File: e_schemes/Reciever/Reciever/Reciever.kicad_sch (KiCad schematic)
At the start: 31 parts, among them J1 Conn_01x03, J2 Conn_01x03, Q1 AO3400A, SW1 SW_Push, SW2 SW_Push, SW3 SW_Reload, U1 ESP32-WROOM-32E

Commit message: ADD: Добавлены  электросхемы
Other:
- company: SF-DEV -> (none)
- title: Схема передатчика -> (none)
- moved on the sheet: C1, C2, C3, C4, C5, D1, D2, D3, D4, D5, D6, J1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

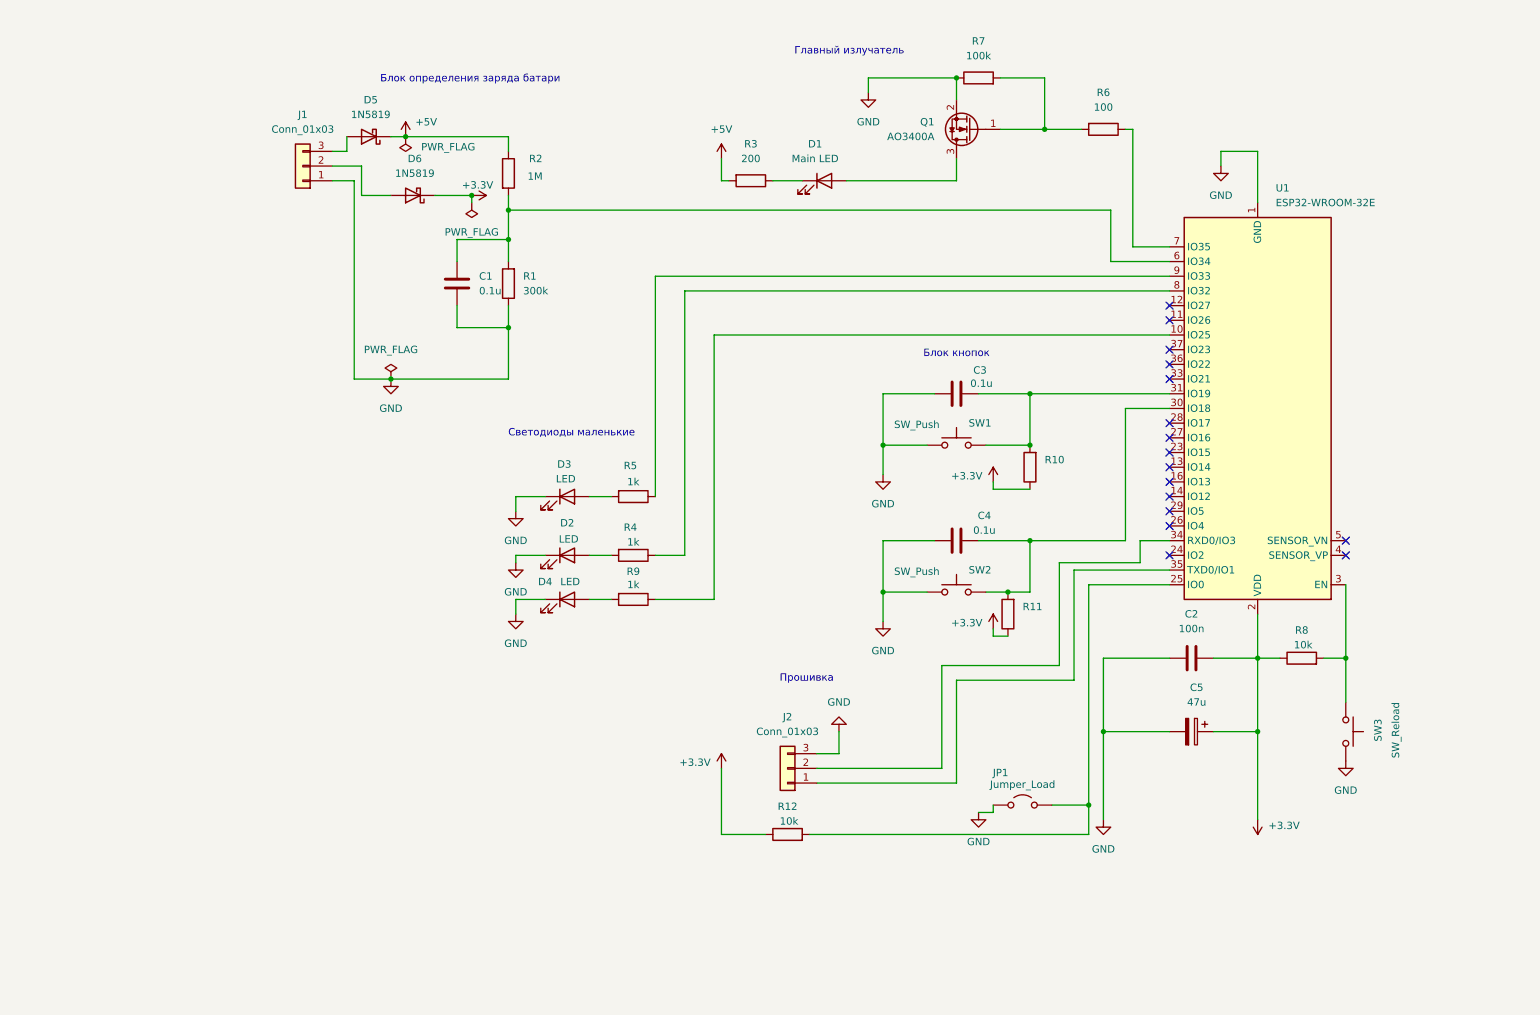
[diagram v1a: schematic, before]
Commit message: ADD:  Схема приемника
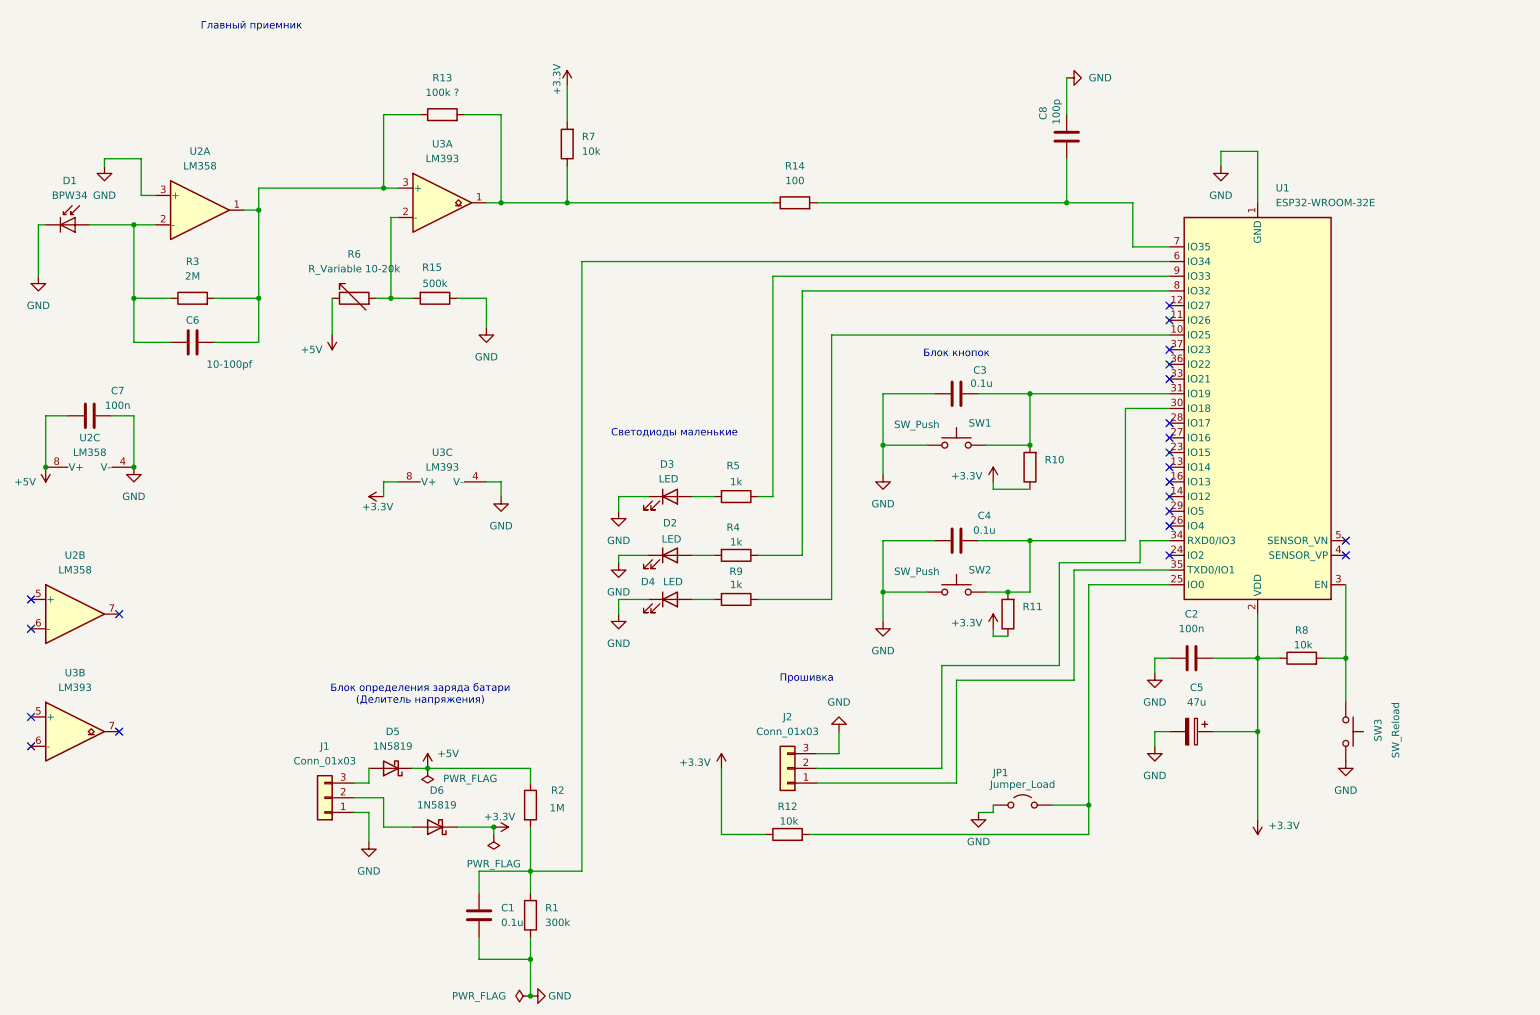
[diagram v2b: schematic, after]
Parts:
- removed D1: Main LED, OptoDevice:Osram_BPW82, symbol Device:LED
- removed Q1: AO3400A, Package_TO_SOT_SMD:SOT-23, symbol Transistor_FET:AO3400A
- removed R6: 100, Resistor_THT:R_Axial_DIN0204_L3.6mm_D1.6mm_P7.62mm_Horizontal, symbol Device:R
- added C6: 10-100pf, Capacitor_THT:C_Disc_D3.0mm_W1.6mm_P2.50mm, symbol Device:C
- added C7: 100n, Capacitor_THT:C_Disc_D3.0mm_W1.6mm_P2.50mm, symbol Device:C
- added C8: 100p, Capacitor_THT:C_Disc_D3.0mm_W1.6mm_P2.50mm, symbol Device:C
- added D1: BPW34, OptoDevice:Osram_DIL2_4.3x4.65mm_P5.08mm, symbol Sensor_Optical:BPW34
- added R13: 100k ?, symbol Device:R
- added R14: 100, symbol Device:R
- added R15: 500k, Resistor_THT:R_Axial_DIN0204_L3.6mm_D1.6mm_P7.62mm_Horizontal, symbol Device:R
- added R6: R_Variable 10-20k, symbol Device:R_Variable
- added U2: LM358, symbol Amplifier_Operational:LM358
- added U3: LM393, symbol Comparator:LM393
- R3: value 200 -> 2M; footprint Resistor_THT:R_Axial_DIN0204_L3.6mm_D1.6mm_P7.62mm_Horizontal -> (none)
- R7: value 100k -> 10k; footprint Resistor_THT:R_Axial_DIN0204_L3.6mm_D1.6mm_P7.62mm_Horizontal -> (none)
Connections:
- net +3.3V: now also R7.2, U3.8 (V+)
- net +5V: now also C7.1, R6.1, U2.8 (V+); no longer R3.2
- net GND: now also C7.2, C8.2, D1.1 (K), R15.1, U2.3 (+), U2.4 (V-), U3.4 (V-); no longer R7.1
- net at U1.7 (IO35): now also C8.1, R14.2
- net at R3.1: now also C6.1, D1.2 (A), U2.2 (-)
- new net: C6.2, R13.1, R3.2, U2.1, U3.3 (+)
- new net: R15.2, R6.2, U3.2 (-)
- new net: R13.2, R14.1, R7.1, U3.1
- no-connect marks 16 -> 22
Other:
- note added: "Блок определения заряда батари (Делитель напряжения)"
- note added: "Главный приемник"
- note removed: "Блок определения заряда батари"
- note removed: "Главный излучатель"
- moved on the sheet: C1, D2, D3, D4, D5, D6, J1, R1, R2, R4, R5, R9

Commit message: UPDATE: схема RX
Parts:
- R13, R14, R3, R6, R7: footprint (none) -> Resistor_THT:R_Axial_DIN0204_L3.6mm_D1.6mm_P7.62mm_Horizontal
- U1: footprint RF_Module:ESP32-WROOM-32E -> RF_Module:ESP32-WROOM-32UE
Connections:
- net at C8.1, R14.2: now also U1.16 (IO13); no longer U1.7 (IO35)
- no-connect marks 22 -> 21
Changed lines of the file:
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@@
 	)
 	(no_connect
-		(at 215.9 95.25)
-	)
-	(no_connect
 		(at 19.05 120.65)
 	)
@@
 	(wire
 		(pts
-			(xy 209.55 46.99) (xy 209.55 54.61)
+			(xy 215.9 95.25) (xy 209.55 95.25)
 		)
 		(stroke
@@
 	(wire
 		(pts
+			(xy 209.55 46.99) (xy 209.55 95.25)
+		)
+		(stroke
+			(width 0)
+			(type default)
+		)
+	)
+	(wire
+		(pts
 			(xy 175.26 80.01) (xy 166.37 80.01)
 		)
@@
 	(wire
 		(pts
-			(xy 209.55 54.61) (xy 215.9 54.61)
-		)
-		(stroke
-			(width 0)
-			(type default)
-		)
-	)
-	(wire
-		(pts
 			(xy 223.52 138.43) (xy 231.14 138.43)
 		)
@@
 			)
 		)
-		(property "Footprint" "RF_Module:ESP32-WROOM-32E"
+		(property "Footprint" "RF_Module:ESP32-WROOM-32UE"
 			(at 214.63 48.26 0)
 			(effects
@@
 			)
 		)
-		(property "Footprint" ""
+		(property "Footprint" "Resistor_THT:R_Axial_DIN0204_L3.6mm_D1.6mm_P7.62mm_Horizontal"
 			(at 151.13 48.768 90)
 			(effects
@@
 			)
 		)
-		(property "Footprint" ""
+		(property "Footprint" "Resistor_THT:R_Axial_DIN0204_L3.6mm_D1.6mm_P7.62mm_Horizontal"
 			(at 90.17 33.528 90)
 			(effects
@@
 			)
 		)
-		(property "Footprint" ""
+		(property "Footprint" "Resistor_THT:R_Axial_DIN0204_L3.6mm_D1.6mm_P7.62mm_Horizontal"
 			(at 74.93 65.278 90)
 			(effects
@@
 			)
 		)
-		(property "Footprint" ""
+		(property "Footprint" "Resistor_THT:R_Axial_DIN0204_L3.6mm_D1.6mm_P7.62mm_Horizontal"
 			(at 113.538 36.83 90)
 			(effects
@@
 			)
 		)
-		(property "Footprint" ""
+		(property "Footprint" "Resistor_THT:R_Axial_DIN0204_L3.6mm_D1.6mm_P7.62mm_Horizontal"
 			(at 46.99 65.278 90)
 			(effects

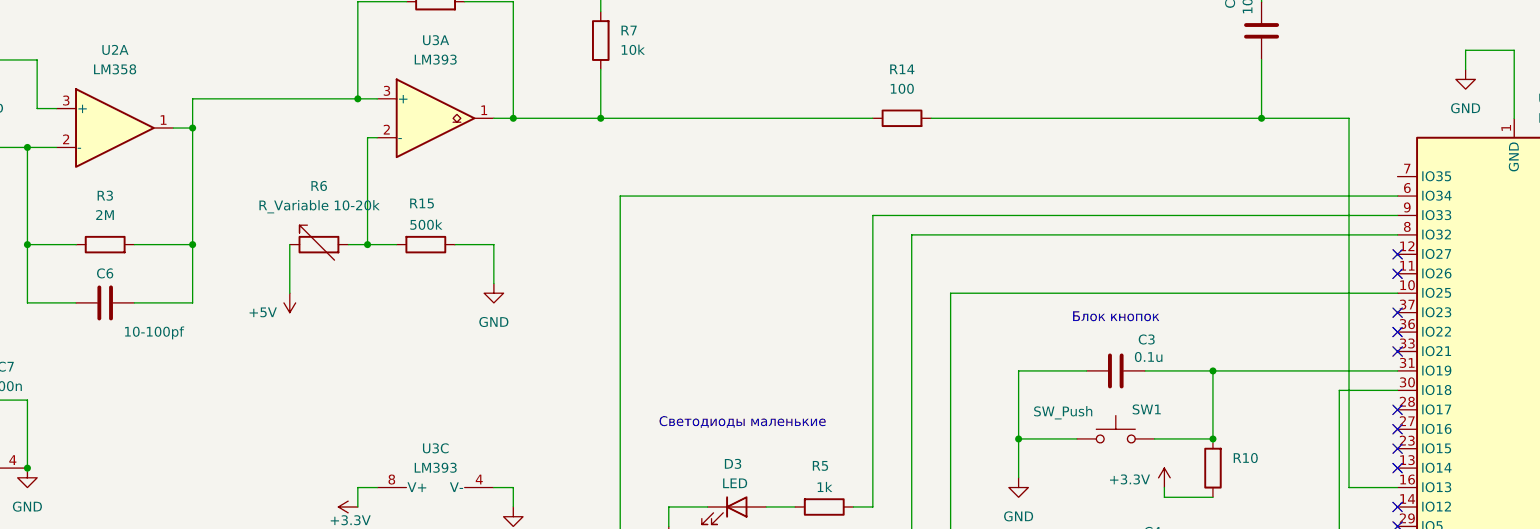
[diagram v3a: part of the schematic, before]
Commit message: Отрисовка схемы
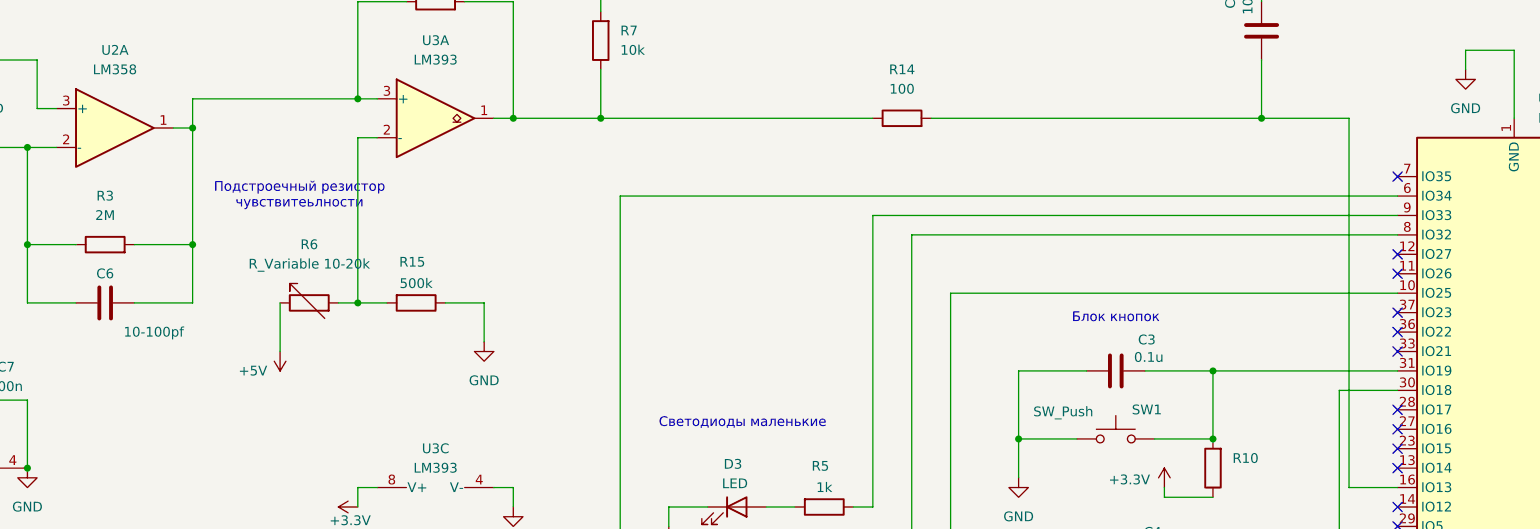
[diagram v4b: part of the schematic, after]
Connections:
- no-connect marks 21 -> 22
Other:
- note added: "Подстроечный резистор чувствитеьлности"
- moved on the sheet: R15, R6
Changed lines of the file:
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@@
 	(generator_version "9.0")
 	(paper "A4")
+	(text "Подстроечный резистор \nчувствитеьлности"
+		(exclude_from_sim no)
+		(at 72.39 57.15 0)
+		(effects
+			(font
+				(size 1.27 1.27)
+			)
+		)
+	)
 	(text "Блок определения заряда батари\n(Делитель напряжения)"
 		(exclude_from_sim no)
@@
 	)
 	(junction
-		(at 81.28 63.5)
+		(at 80.01 71.12)
 		(diameter 0)
 		(color 0 0 0 0)
@@
 	)
 	(no_connect
+		(at 215.9 54.61)
+	)
+	(no_connect
 		(at 215.9 87.63)
 	)
@@
 	(wire
 		(pts
-			(xy 78.74 63.5) (xy 81.28 63.5)
+			(xy 77.47 71.12) (xy 80.01 71.12)
 		)
 		(stroke
@@
 	(wire
 		(pts
-			(xy 81.28 63.5) (xy 85.09 63.5)
+			(xy 80.01 71.12) (xy 83.82 71.12)
 		)
 		(stroke
@@
 	(wire
 		(pts
-			(xy 97.79 68.58) (xy 97.79 63.5)
+			(xy 96.52 76.2) (xy 96.52 71.12)
 		)
 		(stroke
@@
 	(wire
 		(pts
+			(xy 80.01 49.53) (xy 82.55 49.53)
+		)
+		(stroke
+			(width 0)
+			(type default)
+		)
+	)
+	(wire
+		(pts
 			(xy 137.16 107.95) (xy 133.35 107.95)
 		)
@@
 	(wire
 		(pts
-			(xy 71.12 69.85) (xy 71.12 63.5)
+			(xy 69.85 77.47) (xy 69.85 71.12)
 		)
 		(stroke
@@
 	(wire
 		(pts
+			(xy 80.01 49.53) (xy 80.01 71.12)
+		)
+		(stroke
+			(width 0)
+			(type default)
+		)
+	)
+	(wire
+		(pts
 			(xy 100.33 46.99) (xy 100.33 31.75)
 		)
@@
 	(wire
 		(pts
-			(xy 81.28 63.5) (xy 81.28 49.53)
-		)
-		(stroke
-			(width 0)
-			(type default)
-		)
-	)
-	(wire
-		(pts
-			(xy 81.28 49.53) (xy 82.55 49.53)
-		)
-		(stroke
-			(width 0)
-			(type default)
-		)
-	)
-	(wire
-		(pts
 			(xy 80.01 95.25) (xy 82.55 95.25)
 		)
@@
 	(wire
 		(pts
-			(xy 92.71 63.5) (xy 97.79 63.5)
+			(xy 91.44 71.12) (xy 96.52 71.12)
 		)
 		(stroke
@@
 	(symbol
 		(lib_id "power:+5V")
-		(at 71.12 69.85 180)
+		(at 69.85 77.47 180)
 		(unit 1)
 		(exclude_from_sim no)
@@
 		(dnp no)
 		(property "Reference" "#PWR04"
-			(at 71.12 66.04 0)
+			(at 69.85 73.66 0)
 			(effects
 				(font
@@
 		)
 		(property "Value" "+5V"
-			(at 67.564 72.39 0)
+			(at 66.294 80.01 0)
 			(effects
 				(font
@@
 		)
 		(property "Footprint" ""
-			(at 71.12 69.85 0)
+			(at 69.85 77.47 0)
 			(effects
 				(font
@@
 		)
 		(property "Datasheet" ""
-			(at 71.12 69.85 0)
+			(at 69.85 77.47 0)
 			(effects
 				(font
@@
 		)
 		(property "Description" "Power symbol creates a global label with name \"+5V\""
-			(at 71.12 69.85 0)
+			(at 69.85 77.47 0)
 			(effects
 				(font
@@
 	(symbol
 		(lib_id "power:GND")
-		(at 97.79 68.58 0)
+		(at 96.52 76.2 0)
 		(unit 1)
 		(exclude_from_sim no)
@@
 		(fields_autoplaced yes)
 		(property "Reference" "#PWR029"
-			(at 97.79 74.93 0)
+			(at 96.52 82.55 0)
 			(effects
 				(font
@@
 		)
 		(property "Value" "GND"
-			(at 97.79 73.66 0)
+			(at 96.52 81.28 0)
 			(effects
 				(font
@@
 		)
 		(property "Footprint" ""
-			(at 97.79 68.58 0)
+			(at 96.52 76.2 0)
 			(effects
 				(font
@@
 		)
 		(property "Datasheet" ""
-			(at 97.79 68.58 0)
+			(at 96.52 76.2 0)
 			(effects
 				(font
@@
 		)
 		(property "Description" "Power symbol creates a global label with name \"GND\" , ground"
-			(at 97.79 68.58 0)
+			(at 96.52 76.2 0)
 			(effects
 				(font
@@
 	(symbol
 		(lib_id "Device:R")
-		(at 88.9 63.5 270)
+		(at 87.63 71.12 270)
 		(unit 1)
 		(exclude_from_sim no)
@@
 		(dnp no)
 		(property "Reference" "R15"
-			(at 88.392 58.166 90)
+			(at 87.122 65.786 90)
 			(effects
 				(font
@@
 		)
 		(property "Value" "500k"
-			(at 88.9 60.96 90)
+			(at 87.63 68.58 90)
 			(effects
 				(font
@@
 		)
 		(property "Footprint" "Resistor_THT:R_Axial_DIN0204_L3.6mm_D1.6mm_P7.62mm_Horizontal"
-			(at 88.9 61.722 90)
+			(at 87.63 69.342 90)
 			(effects
 				(font
@@
 		)
 		(property "Datasheet" "~"
-			(at 88.9 63.5 0)
+			(at 87.63 71.12 0)
 			(effects
 				(font
@@
 		)
 		(property "Description" "Resistor"
-			(at 88.9 63.5 0)
+			(at 87.63 71.12 0)
 			(effects
 				(font
@@
 	(symbol
 		(lib_id "Device:R_Variable")
-		(at 74.93 63.5 90)
+		(at 73.66 71.12 90)
 		(unit 1)
 		(exclude_from_sim no)
@@
 		(fields_autoplaced yes)
 		(property "Reference" "R6"
-			(at 74.93 55.88 90)
+			(at 73.66 63.5 90)
 			(effects
 				(font
@@
 		)
 		(property "Value" "R_Variable 10-20k"
-			(at 74.93 58.42 90)
+			(at 73.66 66.04 90)
 			(effects
 				(font
@@
 		)
 		(property "Footprint" "Resistor_THT:R_Axial_DIN0204_L3.6mm_D1.6mm_P7.62mm_Horizontal"
-			(at 74.93 65.278 90)
+			(at 73.66 72.898 90)
 			(effects
 				(font
@@
 		)
 		(property "Datasheet" "~"
-			(at 74.93 63.5 0)
+			(at 73.66 71.12 0)
 			(effects
 				(font
@@
 		)
 		(property "Description" "Variable resistor"
-			(at 74.93 63.5 0)
+			(at 73.66 71.12 0)
 			(effects
 				(font
